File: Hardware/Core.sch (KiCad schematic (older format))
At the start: 22 parts, among them U3 AAT1217, U4 MCP6L02T, U5 MSP430G2553-PW28, X2 CRYSTAL

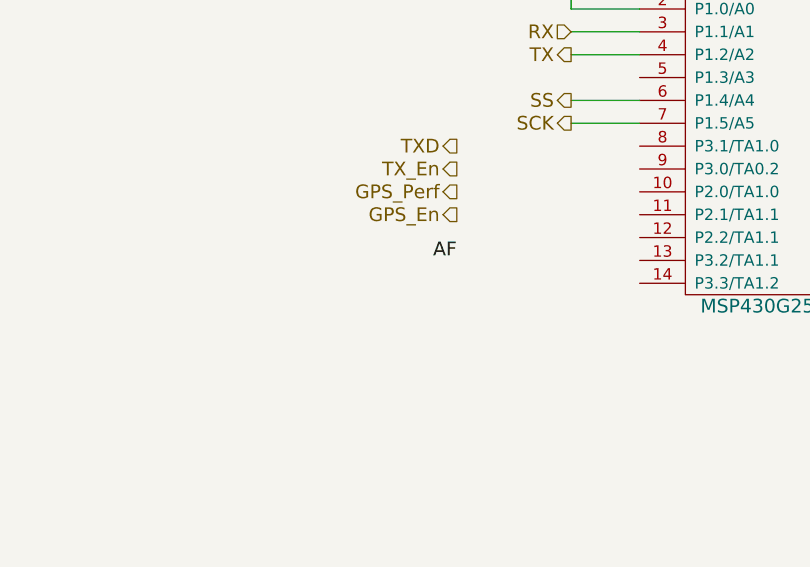
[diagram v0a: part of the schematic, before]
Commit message: Add expansion headers
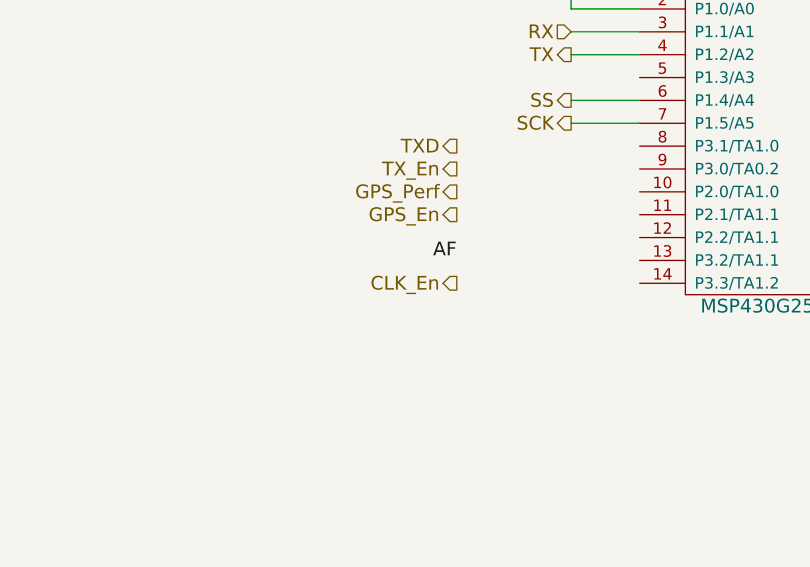
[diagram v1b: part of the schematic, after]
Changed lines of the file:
@@
 Sheet 4 4
 Title "Aether - Pico Tracker"
-Date "4 feb 2014"
+Date "5 feb 2014"
 Rev "1"
 Comp "Aerodyne Labs"
@@
 $EndComp
 $Comp
-L +BATT #PWR041
+L +BATT #PWR045
 U 1 1 52ECD638
 P 1600 1800
-F 0 "#PWR041" H 1600 1750 20  0001 C CNN
+F 0 "#PWR045" H 1600 1750 20  0001 C CNN
 F 1 "+BATT" H 1600 1900 30  0000 C CNN
 F 2 "" H 1600 1800 60  0000 C CNN
@@
 $EndComp
 $Comp
-L GND #PWR042
+L GND #PWR046
 U 1 1 52ECD64A
 P 3600 2700
-F 0 "#PWR042" H 3600 2700 30  0001 C CNN
+F 0 "#PWR046" H 3600 2700 30  0001 C CNN
 F 1 "GND" H 3600 2630 30  0001 C CNN
 F 2 "" H 3600 2700 60  0000 C CNN
@@
 $EndComp
 $Comp
-L GND #PWR043
+L GND #PWR047
 U 1 1 52ECD650
 P 1600 2600
-F 0 "#PWR043" H 1600 2600 30  0001 C CNN
+F 0 "#PWR047" H 1600 2600 30  0001 C CNN
 F 1 "GND" H 1600 2530 30  0001 C CNN
 F 2 "" H 1600 2600 60  0000 C CNN
@@
 $EndComp
 $Comp
-L GND #PWR044
+L GND #PWR048
 U 1 1 52ECD656
 P 2000 2800
-F 0 "#PWR044" H 2000 2800 30  0001 C CNN
+F 0 "#PWR048" H 2000 2800 30  0001 C CNN
 F 1 "GND" H 2000 2730 30  0001 C CNN
 F 2 "" H 2000 2800 60  0000 C CNN
@@
 $EndComp
 $Comp
-L +3.3V #PWR045
+L +3.3V #PWR049
 U 1 1 52ECD663
 P 3600 1800
-F 0 "#PWR045" H 3600 1760 30  0001 C CNN
+F 0 "#PWR049" H 3600 1760 30  0001 C CNN
 F 1 "+3.3V" H 3600 1910 30  0000 C CNN
 F 2 "" H 3600 1800 60  0000 C CNN
@@
 $EndComp
 $Comp
-L GND #PWR046
+L GND #PWR050
 U 1 1 52ECE5C9
 P 8800 4000
-F 0 "#PWR046" H 8800 4000 30  0001 C CNN
+F 0 "#PWR050" H 8800 4000 30  0001 C CNN
 F 1 "GND" H 8800 3930 30  0001 C CNN
 F 2 "" H 8800 4000 60  0000 C CNN
@@
 $EndComp
 $Comp
-L +3.3V #PWR047
+L +3.3V #PWR051
 U 1 1 52ECE681
 P 8900 2000
-F 0 "#PWR047" H 8900 1960 30  0001 C CNN
+F 0 "#PWR051" H 8900 1960 30  0001 C CNN
 F 1 "+3.3V" H 8900 2110 30  0000 C CNN
 F 2 "" H 8900 2000 60  0000 C CNN
@@
 $EndComp
 $Comp
-L +3.3V #PWR048
+L +3.3V #PWR052
 U 1 1 52ECE6CC
 P 7200 2000
-F 0 "#PWR048" H 7200 1960 30  0001 C CNN
+F 0 "#PWR052" H 7200 1960 30  0001 C CNN
 F 1 "+3.3V" H 7200 2110 30  0000 C CNN
 F 2 "" H 7200 2000 60  0000 C CNN
@@
 $EndComp
 $Comp
-L GND #PWR049
+L GND #PWR053
 U 1 1 52ECE742
 P 7900 2200
-F 0 "#PWR049" H 7900 2200 30  0001 C CNN
+F 0 "#PWR053" H 7900 2200 30  0001 C CNN
 F 1 "GND" H 7900 2130 30  0001 C CNN
 F 2 "" H 7900 2200 60  0000 C CNN
@@
 $EndComp
 $Comp
-L GND #PWR050
+L GND #PWR054
 U 1 1 52EDECF2
 P 3100 6500
-F 0 "#PWR050" H 3100 6500 30  0001 C CNN
+F 0 "#PWR054" H 3100 6500 30  0001 C CNN
 F 1 "GND" H 3100 6430 30  0001 C CNN
 F 2 "" H 3100 6500 60  0000 C CNN
@@
 $EndComp
 $Comp
-L GND #PWR051
+L GND #PWR055
 U 1 1 52EDED01
 P 2500 7000
-F 0 "#PWR051" H 2500 7000 30  0001 C CNN
+F 0 "#PWR055" H 2500 7000 30  0001 C CNN
 F 1 "GND" H 2500 6930 30  0001 C CNN
 F 2 "" H 2500 7000 60  0000 C CNN
@@
 $EndComp
 $Comp
-L GND #PWR052
+L GND #PWR056
 U 1 1 52EDF036
 P 5100 6800
-F 0 "#PWR052" H 5100 6800 30  0001 C CNN
+F 0 "#PWR056" H 5100 6800 30  0001 C CNN
 F 1 "GND" H 5100 6730 30  0001 C CNN
 F 2 "" H 5100 6800 60  0000 C CNN
@@
 $EndComp
 $Comp
-L GND #PWR053
+L GND #PWR057
 U 1 1 52EDF155
 P 1800 5500
-F 0 "#PWR053" H 1800 5500 30  0001 C CNN
+F 0 "#PWR057" H 1800 5500 30  0001 C CNN
 F 1 "GND" H 1800 5430 30  0001 C CNN
 F 2 "" H 1800 5500 60  0000 C CNN
@@
 Connection ~ 6300 5800
 $Comp
-L +3.3V #PWR054
+L +3.3V #PWR058
 U 1 1 52EDF302
 P 3100 5300
-F 0 "#PWR054" H 3100 5260 30  0001 C CNN
+F 0 "#PWR058" H 3100 5260 30  0001 C CNN
 F 1 "+3.3V" H 3100 5410 30  0000 C CNN
 F 2 "" H 3100 5300 60  0000 C CNN
@@
 Connection ~ 4800 1700
 $Comp
-L GND #PWR055
+L GND #PWR059
 U 1 1 52EF30D2
 P 5500 2400
-F 0 "#PWR055" H 5500 2400 30  0001 C CNN
+F 0 "#PWR059" H 5500 2400 30  0001 C CNN
 F 1 "GND" H 5500 2330 30  0001 C CNN
 F 2 "" H 5500 2400 60  0000 C CNN
@@
 $EndComp
 $Comp
-L GND #PWR056
+L GND #PWR060
 U 1 1 52EF30E1
 P 4800 2400
-F 0 "#PWR056" H 4800 2400 30  0001 C CNN
+F 0 "#PWR060" H 4800 2400 30  0001 C CNN
 F 1 "GND" H 4800 2330 30  0001 C CNN
 F 2 "" H 4800 2400 60  0000 C CNN
@@
 Stat
 $Comp
-L +BATT #PWR057
+L +BATT #PWR061
 U 1 1 52EFA84C
 P 7000 2200
-F 0 "#PWR057" H 7000 2150 20  0001 C CNN
+F 0 "#PWR061" H 7000 2150 20  0001 C CNN
 F 1 "+BATT" H 7000 2300 30  0000 C CNN
 F 2 "" H 7000 2200 60  0000 C CNN
@@
 	1    0    0    -1
 $EndComp
+Text HLabel 6500 3900 0    60   Output ~ 0
+CLK_En
 $EndSCHEMATC

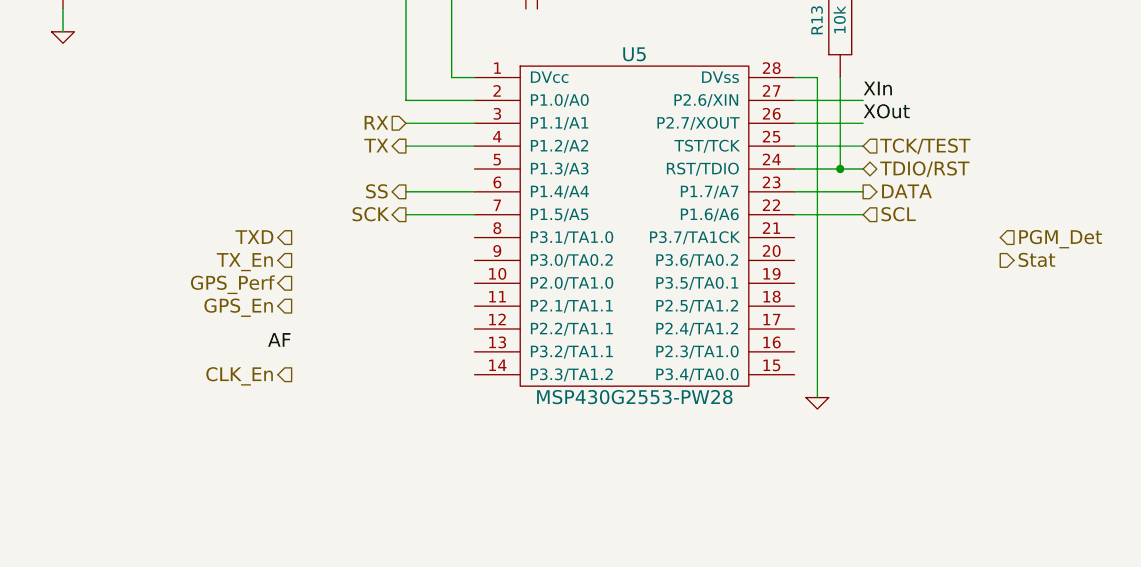
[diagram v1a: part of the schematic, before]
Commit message: Change to soft SPI, routing
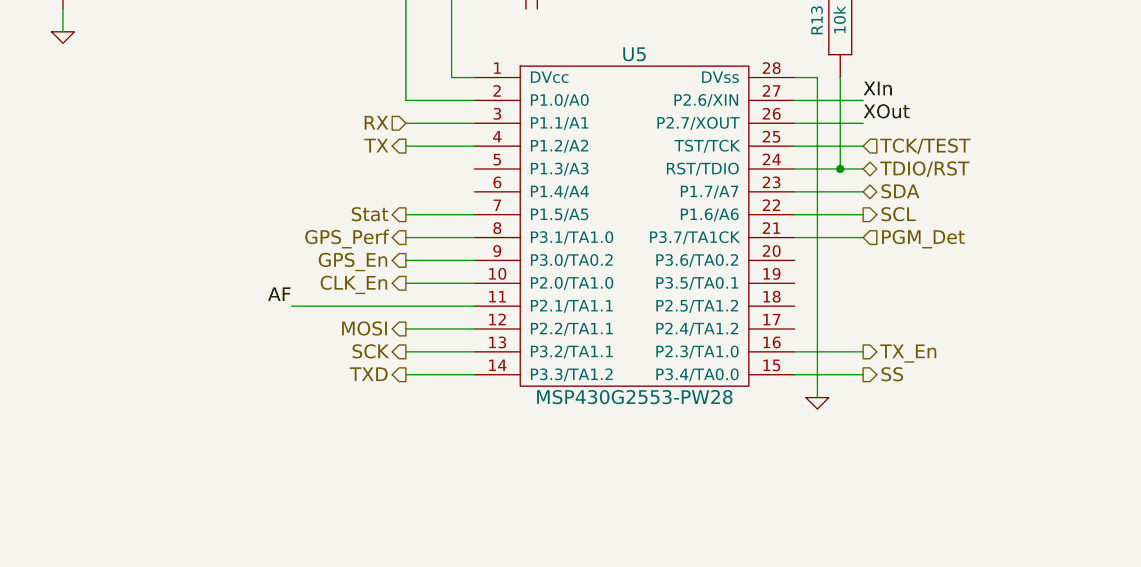
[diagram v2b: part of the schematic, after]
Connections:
- net AF: now also U5.11 (P2.1/TA1.1)
- net CLK_En: now also U5.10 (P2.0/TA1.0)
- net GPS_En: now also U5.9 (P3.0/TA0.2)
- net GPS_Perf: now also U5.8 (P3.1/TA1.0)
- net PGM_Det: now also U5.21 (P3.7/TA1CK)
- net SCK: now also U5.13 (P3.2/TA1.1); no longer U5.7 (P1.5/A5)
- net SS: now also U5.15 (P3.4/TA0.0); no longer U5.6 (P1.4/A4)
- net Stat: now also U5.7 (P1.5/A5)
- net TXD: now also U5.14 (P3.3/TA1.2)
- net TX_En: now also U5.16 (P2.3/TA1.0)
- net MOSI: now reaches U5.12 (P2.2/TA1.1)
- net DATA renamed SDA
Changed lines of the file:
@@
 Text HLabel 7000 2900 0    60   Output ~ 0
 TX
-Text HLabel 6500 3600 0    60   Output ~ 0
+Text HLabel 7000 3400 0    60   Output ~ 0
 GPS_En
-Text HLabel 9000 3100 2    60   Output ~ 0
-DATA
-Text HLabel 7000 3200 0    60   Output ~ 0
+Text HLabel 7000 3800 0    60   Output ~ 0
 SCK
-Text HLabel 7000 3100 0    60   Output ~ 0
+Text HLabel 9000 3900 2    60   Output ~ 0
 SS
-Text HLabel 6500 3400 0    60   Output ~ 0
+Text HLabel 9000 3800 2    60   Output ~ 0
 TX_En
-Text HLabel 6500 3300 0    60   Output ~ 0
+Text HLabel 7000 3900 0    60   Output ~ 0
 TXD
 Text HLabel 6400 5800 2    60   Output ~ 0
@@
 Text HLabel 9000 2900 2    60   Input ~ 0
 TCK/TEST
-Text HLabel 9600 3300 2    60   Input ~ 0
+Text HLabel 9000 3300 2    60   Input ~ 0
 PGM_Det
 $Comp
@@
 	9000 3100 8700 3100
 Wire Wire Line
-	7000 3100 7300 3100
-Wire Wire Line
-	7000 3200 7300 3200
-Wire Wire Line
 	2500 6800 2500 7000
 Wire Wire Line
@@
 Wire Wire Line
 	1100 6200 1200 6200
-Text Label 6500 3800 2    60   ~ 0
+Text Label 6500 3600 2    60   ~ 0
 AF
-Text HLabel 6500 3500 0    60   Output ~ 0
+Text HLabel 7000 3300 0    60   Output ~ 0
 GPS_Perf
 $Comp
@@
 	1    0    0    -1
 $EndComp
-Text HLabel 9000 3200 2    60   Input ~ 0
+Text HLabel 9000 3200 2    60   Output ~ 0
 SCL
 Wire Wire Line
@@
 	1    0    0    -1
 $EndComp
-Text HLabel 9600 3400 2    60   Output ~ 0
+Text HLabel 7000 3200 0    60   Output ~ 0
 Stat
 $Comp
@@
 	1    0    0    -1
 $EndComp
-Text HLabel 6500 3900 0    60   Output ~ 0
+Text HLabel 7000 3500 0    60   Output ~ 0
 CLK_En
+Wire Wire Line
+	9000 3300 8700 3300
+Wire Wire Line
+	7000 3300 7300 3300
+Wire Wire Line
+	7000 3400 7300 3400
+Wire Wire Line
+	8700 3800 9000 3800
+Wire Wire Line
+	8700 3900 9000 3900
+Wire Wire Line
+	7000 3800 7300 3800
+Wire Wire Line
+	7000 3900 7300 3900
+Text HLabel 9000 3100 2    60   BiDi ~ 0
+SDA
+Text HLabel 7000 3700 0    60   Output ~ 0
+MOSI
+Wire Wire Line
+	6500 3600 7300 3600
+Wire Wire Line
+	7000 3700 7300 3700
+Wire Wire Line
+	7000 3200 7300 3200
+Wire Wire Line
+	7000 3500 7300 3500
 $EndSCHEMATC

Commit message: Additional layout
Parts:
- added R14: 10k, ~, symbol R
- X2: value CRYSTAL -> 8MHz; Distributor Part No (none) -> 535-10630-1-ND
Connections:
- net PGM_Det: now also R14.1; no longer U5.21 (P3.7/TA1CK)
- new net: R14.2, U5.21 (P3.7/TA1CK)
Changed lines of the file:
@@
 Sheet 4 4
 Title "Aether - Pico Tracker"
-Date "5 feb 2014"
+Date "6 feb 2014"
 Rev "1"
 Comp "Aerodyne Labs"
@@
 Text HLabel 9000 2900 2    60   Input ~ 0
 TCK/TEST
-Text HLabel 9000 3300 2    60   Input ~ 0
+Text HLabel 9500 3300 2    60   Input ~ 0
 PGM_Det
 $Comp
@@
 P 5150 1700
 F 0 "X2" H 5150 1850 60  0000 C CNN
-F 1 "CRYSTAL" H 5150 1550 60  0000 C CNN
+F 1 "8MHz" H 5150 1550 60  0000 C CNN
 F 2 "~" H 5150 1700 60  0000 C CNN
 F 3 "~" H 5150 1700 60  0000 C CNN
+F 4 "535-10630-1-ND" H 5150 1700 60  0001 C CNN "Distributor Part No"
 	1    5150 1700
 	1    0    0    -1
@@
 Wire Wire Line
 	7000 3500 7300 3500
+$Comp
+L R R14
+U 1 1 52F2E641
+P 9250 3300
+F 0 "R14" H 9250 3400 50  0000 C CNN
+F 1 "10k" H 9250 3300 50  0000 C CNN
+F 2 "~" H 9250 3300 60  0000 C CNN
+F 3 "~" H 9250 3300 60  0000 C CNN
+F 4 "W" H 9250 3200 50  0001 C CNN "Power"
+F 5 "%" H 9250 3100 50  0001 C CNN "Tolerance"
+	1    9250 3300
+	-1   0    0    1
+$EndComp
 $EndSCHEMATC

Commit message: Optimize some values
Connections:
- net GPS_En: now also U5.8 (P3.1/TA1.0); no longer U5.9 (P3.0/TA0.2)
- net GPS_Perf: now also U5.7 (P1.5/A5); no longer U5.8 (P3.1/TA1.0)
- net Stat: now also U5.9 (P3.0/TA0.2); no longer U5.7 (P1.5/A5)
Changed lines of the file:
@@
 $EndComp
 $Comp
-L +BATT #PWR045
+L +BATT #PWR048
 U 1 1 52ECD638
 P 1600 1800
-F 0 "#PWR045" H 1600 1750 20  0001 C CNN
+F 0 "#PWR048" H 1600 1750 20  0001 C CNN
 F 1 "+BATT" H 1600 1900 30  0000 C CNN
 F 2 "" H 1600 1800 60  0000 C CNN
@@
 $EndComp
 $Comp
-L GND #PWR046
+L GND #PWR049
 U 1 1 52ECD64A
 P 3600 2700
-F 0 "#PWR046" H 3600 2700 30  0001 C CNN
+F 0 "#PWR049" H 3600 2700 30  0001 C CNN
 F 1 "GND" H 3600 2630 30  0001 C CNN
 F 2 "" H 3600 2700 60  0000 C CNN
@@
 $EndComp
 $Comp
-L GND #PWR047
+L GND #PWR050
 U 1 1 52ECD650
 P 1600 2600
-F 0 "#PWR047" H 1600 2600 30  0001 C CNN
+F 0 "#PWR050" H 1600 2600 30  0001 C CNN
 F 1 "GND" H 1600 2530 30  0001 C CNN
 F 2 "" H 1600 2600 60  0000 C CNN
@@
 $EndComp
 $Comp
-L GND #PWR048
+L GND #PWR051
 U 1 1 52ECD656
 P 2000 2800
-F 0 "#PWR048" H 2000 2800 30  0001 C CNN
+F 0 "#PWR051" H 2000 2800 30  0001 C CNN
 F 1 "GND" H 2000 2730 30  0001 C CNN
 F 2 "" H 2000 2800 60  0000 C CNN
@@
 $EndComp
 $Comp
-L +3.3V #PWR049
+L +3.3V #PWR052
 U 1 1 52ECD663
 P 3600 1800
-F 0 "#PWR049" H 3600 1760 30  0001 C CNN
+F 0 "#PWR052" H 3600 1760 30  0001 C CNN
 F 1 "+3.3V" H 3600 1910 30  0000 C CNN
 F 2 "" H 3600 1800 60  0000 C CNN
@@
 $EndComp
 $Comp
-L GND #PWR050
+L GND #PWR053
 U 1 1 52ECE5C9
 P 8800 4000
-F 0 "#PWR050" H 8800 4000 30  0001 C CNN
+F 0 "#PWR053" H 8800 4000 30  0001 C CNN
 F 1 "GND" H 8800 3930 30  0001 C CNN
 F 2 "" H 8800 4000 60  0000 C CNN
@@
 $EndComp
 $Comp
-L +3.3V #PWR051
+L +3.3V #PWR054
 U 1 1 52ECE681
 P 8900 2000
-F 0 "#PWR051" H 8900 1960 30  0001 C CNN
+F 0 "#PWR054" H 8900 1960 30  0001 C CNN
 F 1 "+3.3V" H 8900 2110 30  0000 C CNN
 F 2 "" H 8900 2000 60  0000 C CNN
@@
 $EndComp
 $Comp
-L +3.3V #PWR052
+L +3.3V #PWR055
 U 1 1 52ECE6CC
 P 7200 2000
-F 0 "#PWR052" H 7200 1960 30  0001 C CNN
+F 0 "#PWR055" H 7200 1960 30  0001 C CNN
 F 1 "+3.3V" H 7200 2110 30  0000 C CNN
 F 2 "" H 7200 2000 60  0000 C CNN
@@
 $EndComp
 $Comp
-L GND #PWR053
+L GND #PWR056
 U 1 1 52ECE742
 P 7900 2200
-F 0 "#PWR053" H 7900 2200 30  0001 C CNN
+F 0 "#PWR056" H 7900 2200 30  0001 C CNN
 F 1 "GND" H 7900 2130 30  0001 C CNN
 F 2 "" H 7900 2200 60  0000 C CNN
@@
 Text HLabel 7000 2900 0    60   Output ~ 0
 TX
-Text HLabel 7000 3400 0    60   Output ~ 0
+Text HLabel 7000 3300 0    60   Output ~ 0
 GPS_En
 Text HLabel 7000 3800 0    60   Output ~ 0
@@
 $EndComp
 $Comp
-L GND #PWR054
+L GND #PWR057
 U 1 1 52EDECF2
 P 3100 6500
-F 0 "#PWR054" H 3100 6500 30  0001 C CNN
+F 0 "#PWR057" H 3100 6500 30  0001 C CNN
 F 1 "GND" H 3100 6430 30  0001 C CNN
 F 2 "" H 3100 6500 60  0000 C CNN
@@
 $EndComp
 $Comp
-L GND #PWR055
+L GND #PWR058
 U 1 1 52EDED01
 P 2500 7000
-F 0 "#PWR055" H 2500 7000 30  0001 C CNN
+F 0 "#PWR058" H 2500 7000 30  0001 C CNN
 F 1 "GND" H 2500 6930 30  0001 C CNN
 F 2 "" H 2500 7000 60  0000 C CNN
@@
 $EndComp
 $Comp
-L GND #PWR056
+L GND #PWR059
 U 1 1 52EDF036
 P 5100 6800
-F 0 "#PWR056" H 5100 6800 30  0001 C CNN
+F 0 "#PWR059" H 5100 6800 30  0001 C CNN
 F 1 "GND" H 5100 6730 30  0001 C CNN
 F 2 "" H 5100 6800 60  0000 C CNN
@@
 $EndComp
 $Comp
-L GND #PWR057
+L GND #PWR060
 U 1 1 52EDF155
 P 1800 5500
-F 0 "#PWR057" H 1800 5500 30  0001 C CNN
+F 0 "#PWR060" H 1800 5500 30  0001 C CNN
 F 1 "GND" H 1800 5430 30  0001 C CNN
 F 2 "" H 1800 5500 60  0000 C CNN
@@
 Connection ~ 6300 5800
 $Comp
-L +3.3V #PWR058
+L +3.3V #PWR061
 U 1 1 52EDF302
 P 3100 5300
-F 0 "#PWR058" H 3100 5260 30  0001 C CNN
+F 0 "#PWR061" H 3100 5260 30  0001 C CNN
 F 1 "+3.3V" H 3100 5410 30  0000 C CNN
 F 2 "" H 3100 5300 60  0000 C CNN
@@
 Text Label 6500 3600 2    60   ~ 0
 AF
-Text HLabel 7000 3300 0    60   Output ~ 0
+Text HLabel 7000 3200 0    60   Output ~ 0
 GPS_Perf
 $Comp
@@
 Connection ~ 4800 1700
 $Comp
-L GND #PWR059
+L GND #PWR062
 U 1 1 52EF30D2
 P 5500 2400
-F 0 "#PWR059" H 5500 2400 30  0001 C CNN
+F 0 "#PWR062" H 5500 2400 30  0001 C CNN
 F 1 "GND" H 5500 2330 30  0001 C CNN
 F 2 "" H 5500 2400 60  0000 C CNN
@@
 $EndComp
 $Comp
-L GND #PWR060
+L GND #PWR063
 U 1 1 52EF30E1
 P 4800 2400
-F 0 "#PWR060" H 4800 2400 30  0001 C CNN
+F 0 "#PWR063" H 4800 2400 30  0001 C CNN
 F 1 "GND" H 4800 2330 30  0001 C CNN
 F 2 "" H 4800 2400 60  0000 C CNN
@@
 	1    0    0    -1
 $EndComp
-Text HLabel 7000 3200 0    60   Output ~ 0
+Text HLabel 7000 3400 0    60   Output ~ 0
 Stat
 $Comp
-L +BATT #PWR061
+L +BATT #PWR064
 U 1 1 52EFA84C
 P 7000 2200
-F 0 "#PWR061" H 7000 2150 20  0001 C CNN
+F 0 "#PWR064" H 7000 2150 20  0001 C CNN
 F 1 "+BATT" H 7000 2300 30  0000 C CNN
 F 2 "" H 7000 2200 60  0000 C CNN
